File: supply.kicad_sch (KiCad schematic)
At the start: 0 parts

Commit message: added hierachical sheets
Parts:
- added C1, C2, C5, C6, C7, C8: C_Small, symbol Device:C_Small
- added IC3: BQ25622ERYKR, ARMband:BQ25620RYKR, symbol ARMband:BQ25622ERYKR
- added IC4: BQ27427YZFR, ARMband:BGA9C50P3X3_158X162X62, symbol ARMband:BQ27427YZFR
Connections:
- new net +1V8: C7.1, C8.1
- new net +3V3: C5.1, C6.1
- new net +5V: C1.1, C2.1
- new net CHRG_CE: IC3.14 (~{CE})
- new net CHRG_INT: IC3.11 (~{INT})
- new net CHRG_PG: IC3.3 (~{PG})
- new net CHRG_STAT: IC3.10 (STAT)
- new net GASG_BIN: IC4.B1 (BIN)
- new net GASG_GPOUT: IC4.A1 (GPOUT)
- new net GND: C1.2, C2.2, C5.2, C6.2, C7.2, C8.2, IC3.15 (GND), IC4.B2 (VSS_1), IC4.C1 (VSS_2)
- new net I2C_SCL: IC3.13 (SCL), IC4.A3 (SCL)
- new net I2C_SDA: IC3.12 (SDA), IC4.A2 (SDA)

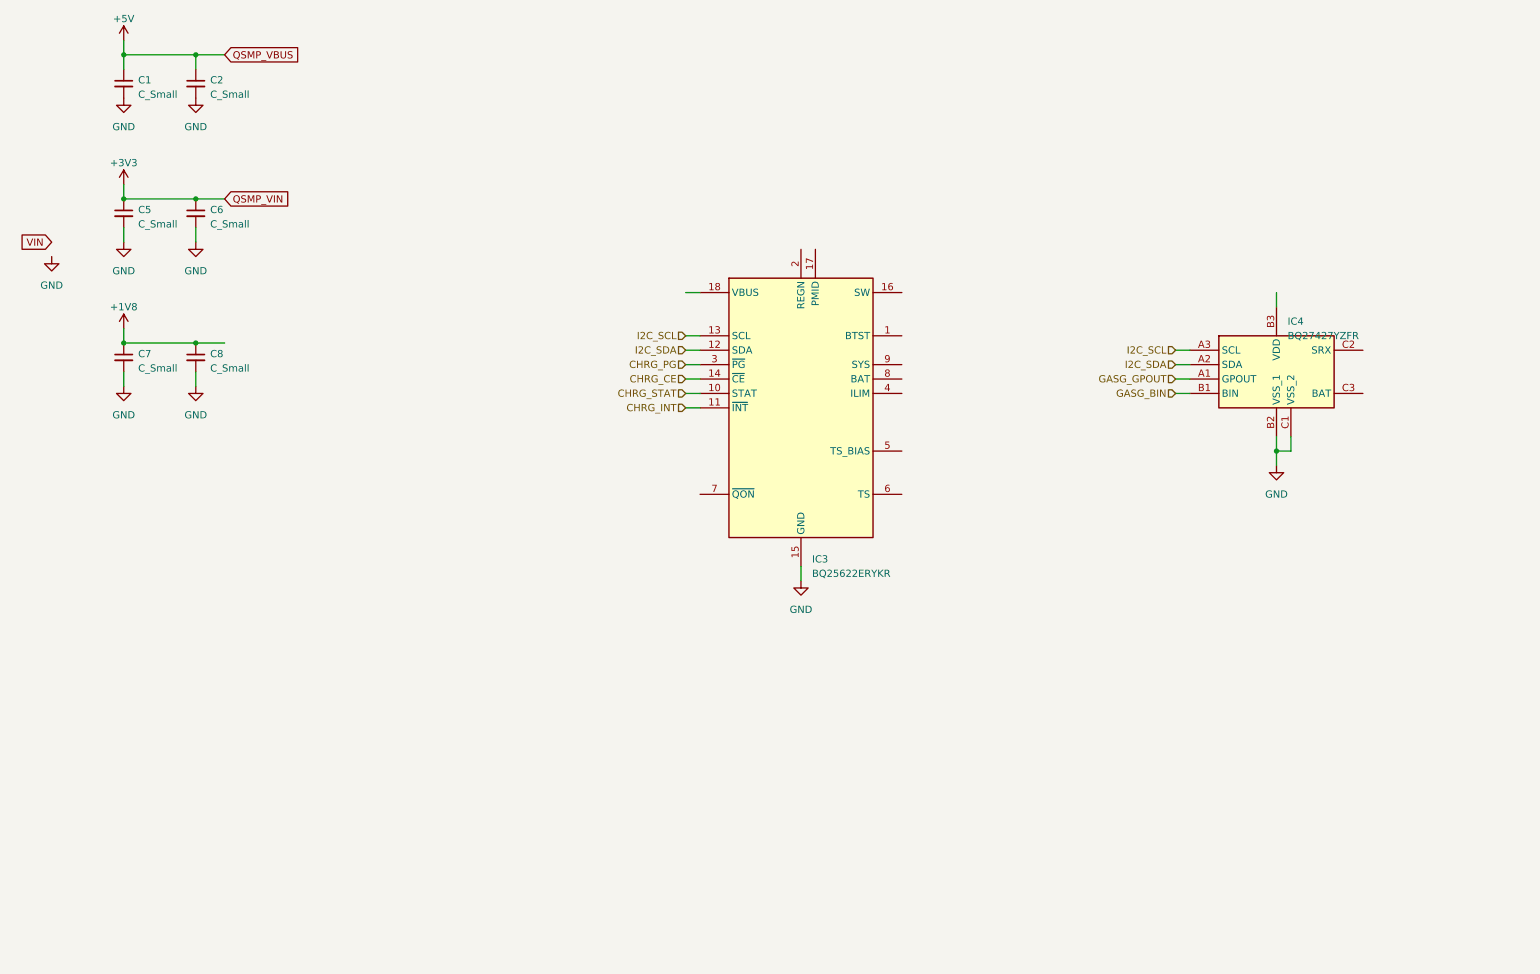
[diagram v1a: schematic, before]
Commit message: progressed charging and gas gauge schematic
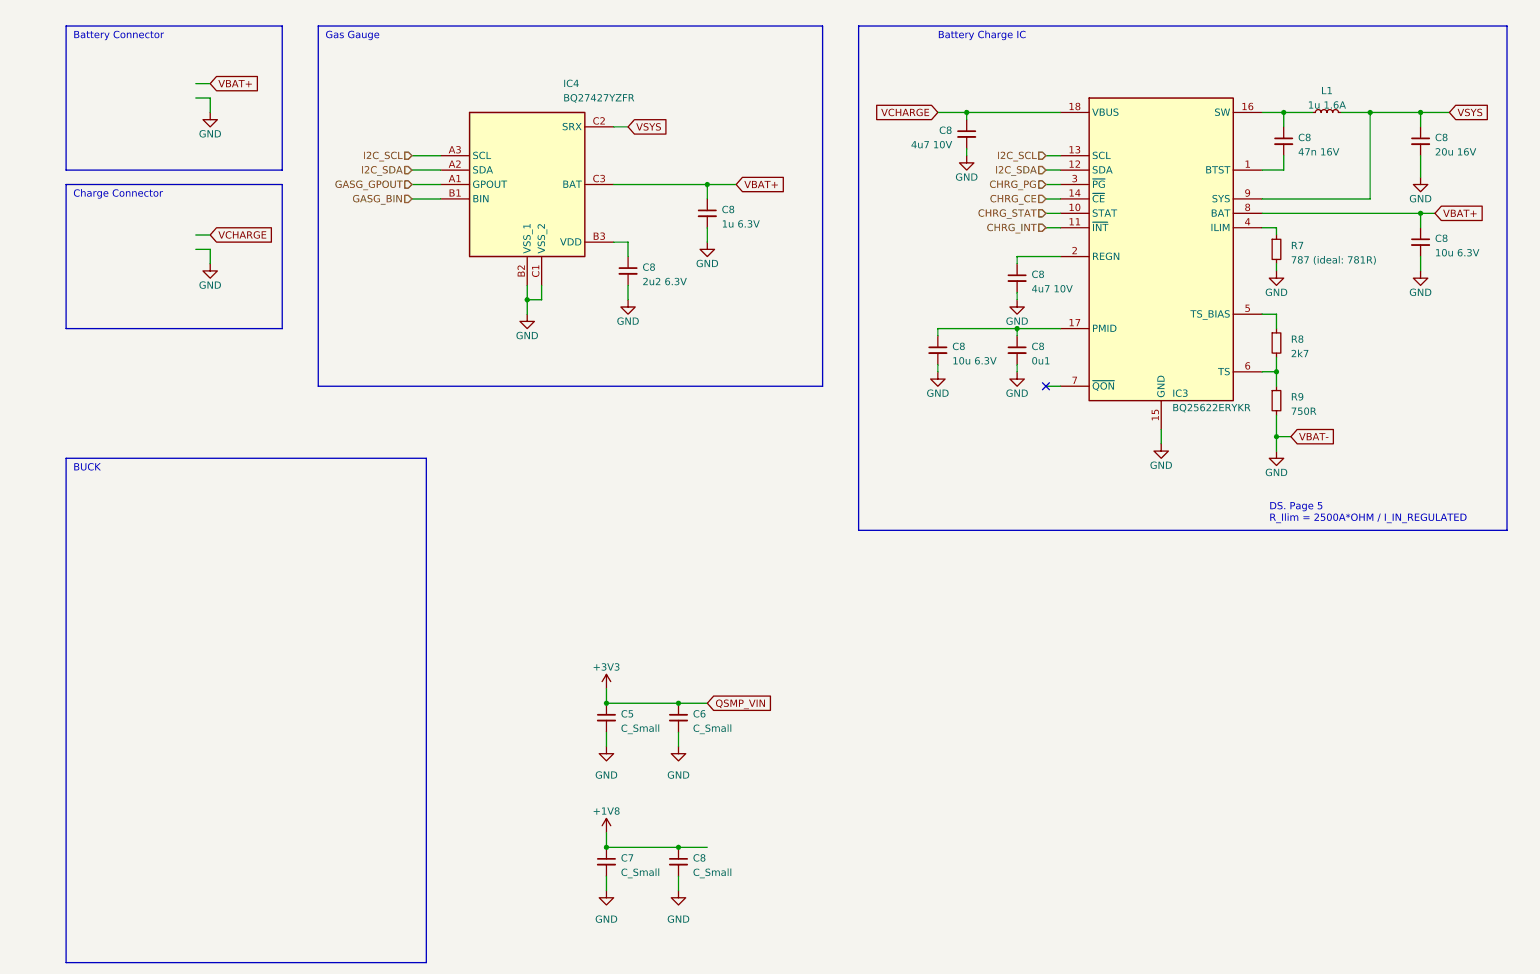
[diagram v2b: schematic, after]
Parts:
- removed C1, C2: C_Small, symbol Device:C_Small
- added C8: 20u 16V, ARMband:C_0704, symbol Device:C_Small
- added C8: 0u1, symbol Device:C_Small
- added C8: 47n 16V, Capacitor_SMD:C_0201_0603Metric, symbol Device:C_Small
- added C8 (x2): 4u7 10V, Capacitor_SMD:C_0402_1005Metric, symbol Device:C_Small
- added C8: 2u2 6.3V, Capacitor_SMD:C_0201_0603Metric, symbol Device:C_Small
- added C8 (x2): 10u 6.3V, Capacitor_SMD:C_0402_1005Metric, symbol Device:C_Small
- added C8: 1u 6.3V, Capacitor_SMD:C_0201_0603Metric, symbol Device:C_Small
- added L1: 1u 1.6A, Inductor_SMD:L_0603_1608Metric, symbol Device:L_Small
- added R7: 787 (ideal: 781R), Resistor_SMD:R_0201_0603Metric, symbol Device:R_Small
- added R8: 2k7, symbol Device:R_Small
- added R9: 750R, symbol Device:R_Small
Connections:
- net GND: now also C8.2, C8.2, C8.2, C8.2, C8.2, C8.2, C8.2, C8.2, R7.2, R9.2
- net at IC4.B3 (VDD): now also C8.1
- net VSYS: now reaches IC4.C2 (SRX)
- net VSYS: now also IC3.9 (SYS), C8.1, L1.2
- net VBAT+: now reaches IC4.C3 (BAT)
- net VBAT+: now also IC3.8 (BAT), C8.1, C8.1
- net at IC3.1 (BTST): now also C8.2
- net at IC3.16 (SW): now also C8.1, L1.1
- net at IC3.17 (PMID): now also C8.1, C8.1
- net VCHARGE: now reaches IC3.18 (VBUS)
- net VCHARGE: now also C8.1
- net at IC3.2 (REGN): now also C8.1
- net at IC3.4 (ILIM): now also R7.1
- net at IC3.5 (TS_BIAS): now also R8.1
- net at IC3.6 (TS): now also R8.2, R9.1
- no-connect marks 0 -> 1
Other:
- note added: "BUCK"
- note added: "Battery Charge IC"
- note added: "Battery Connector"
- note added: "Charge Connector"
- note added: "DS. Page 5 R_Ilim = 2500A*OHM / I_IN_REGULATED"
- note added: "Gas Gauge"
- moved on the sheet: C5, C6, C7, C8, IC3, IC4

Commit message: added buck
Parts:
- removed C5, C6, C7, C8: C_Small, symbol Device:C_Small
- added C7 (x2): 22u, symbol Device:C_Small
- added C7: 22u, Capacitor_SMD:C_0402_1005Metric, symbol Device:C_Small
- added IC3: TPS62410DRCR, ARMband:LM5165XQDRCRQ1, symbol ARMband:TPS62410DRCR
- added L1, L2: 4u7, Inductor_SMD:L_Bourns-SRN4018, symbol Device:L_Small
- added R10: 180k, Resistor_SMD:R_0201_0603Metric, symbol Device:R_Small
- added R14: 0R, Resistor_SMD:R_0201_0603Metric, symbol Device:R_Small
- added R2 (x2): 10k, Resistor_SMD:R_0201_0603Metric_Pad0.64x0.40mm_HandSolder, symbol Device:R_Small
- added R7: 680k, Resistor_SMD:R_0201_0603Metric, symbol Device:R_Small
- added R8: 150k, Resistor_SMD:R_0201_0603Metric, symbol Device:R_Small
- added R9: 360k, Resistor_SMD:R_0201_0603Metric, symbol Device:R_Small
- renumbered L1 to L3, R7 to R11, R8 to R12, R9 to R13
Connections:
- net +1V8: now also C7.1, C7.1, L2.1, R9.1
- net +3V3: now also C7.1, IC3.4 (FB1), L1.1, R7.1
- net GND: now also C7.2, C7.2, IC3.11 (EP_1), IC3.12 (EP_2), IC3.13 (EP_3), IC3.14 (EP_4), IC3.15 (EP_5), IC3.8 (GND), R10.2, R14.2, R8.2
- net VSYS: now also IC3.3 (VIN), R2.1, R2.1
- new net: IC3.7 (EN1), R2.2
- new net: C7.2, IC3.1 (ADJ2), R10.1, R9.2
- new net: IC3.2 (MODE/DATA), R14.1
- new net: IC3.10 (SW2), L2.2
- new net: IC3.5 (DEF_1), R7.2, R8.1
- new net: IC3.6 (SW1), L1.2
- new net: IC3.9 (EN2), R2.2
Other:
- note added: "Vref = 0.6V 1.8V Rail probably heavy ripple current due to low load"

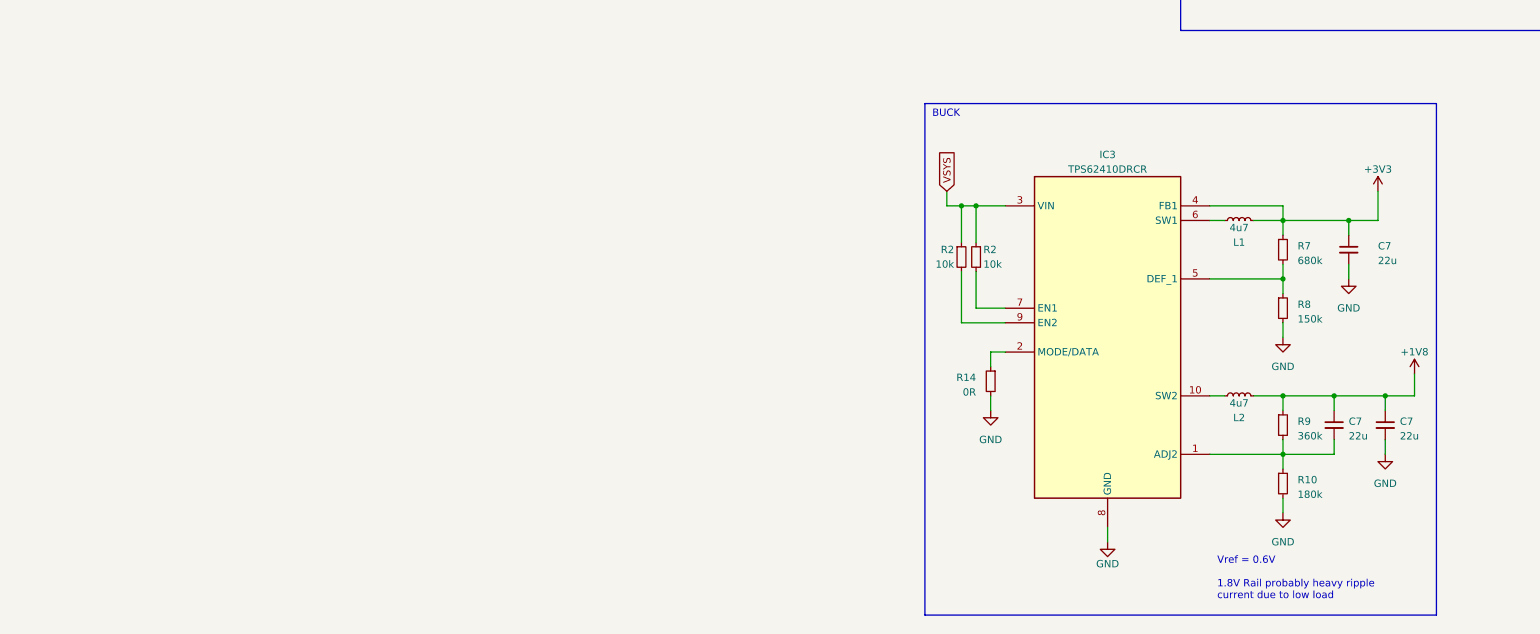
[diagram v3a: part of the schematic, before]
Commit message: added new bucks
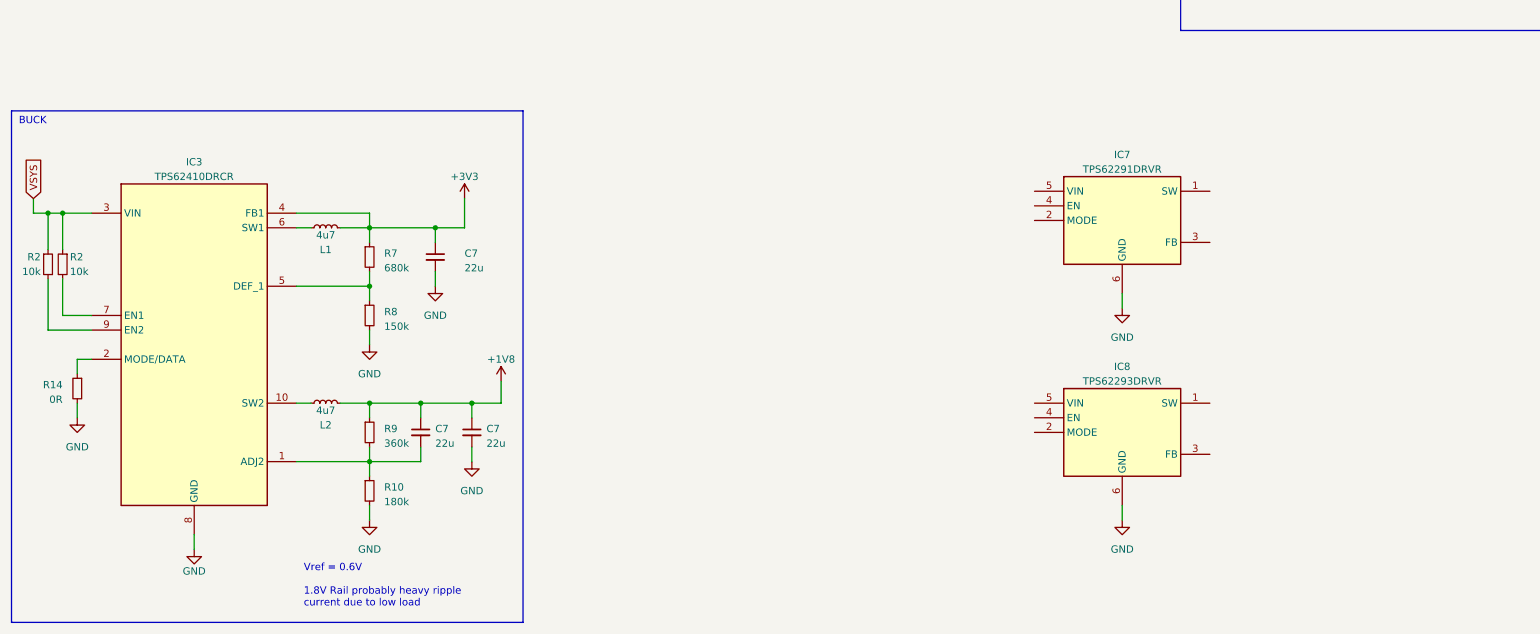
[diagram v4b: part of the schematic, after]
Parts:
- added IC7: TPS62291DRVR, ARMband:SON65P200X200X80-7N, symbol ARMband:TPS62291DRVR
- added IC8: TPS62293DRVR, ARMband:SON65P200X200X80-7N, symbol ARMband:TPS62293DRVR
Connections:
- net GND renamed EP
- net EP: now also IC7.6 (GND), IC7.7 (EP), IC8.6 (GND), IC8.7 (EP)
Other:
- moved on the sheet: C7, IC3, L1, L2, R10, R14, R2, R7, R8, R9

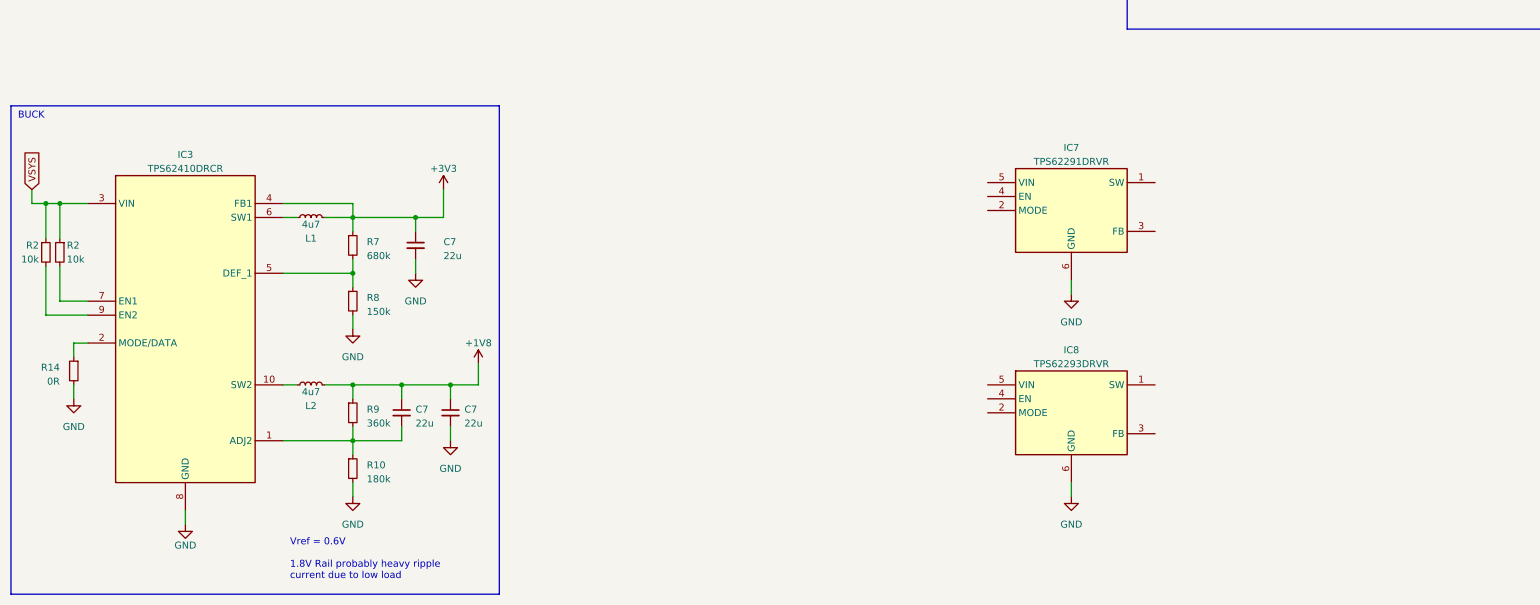
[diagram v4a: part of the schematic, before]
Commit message: buck circuits
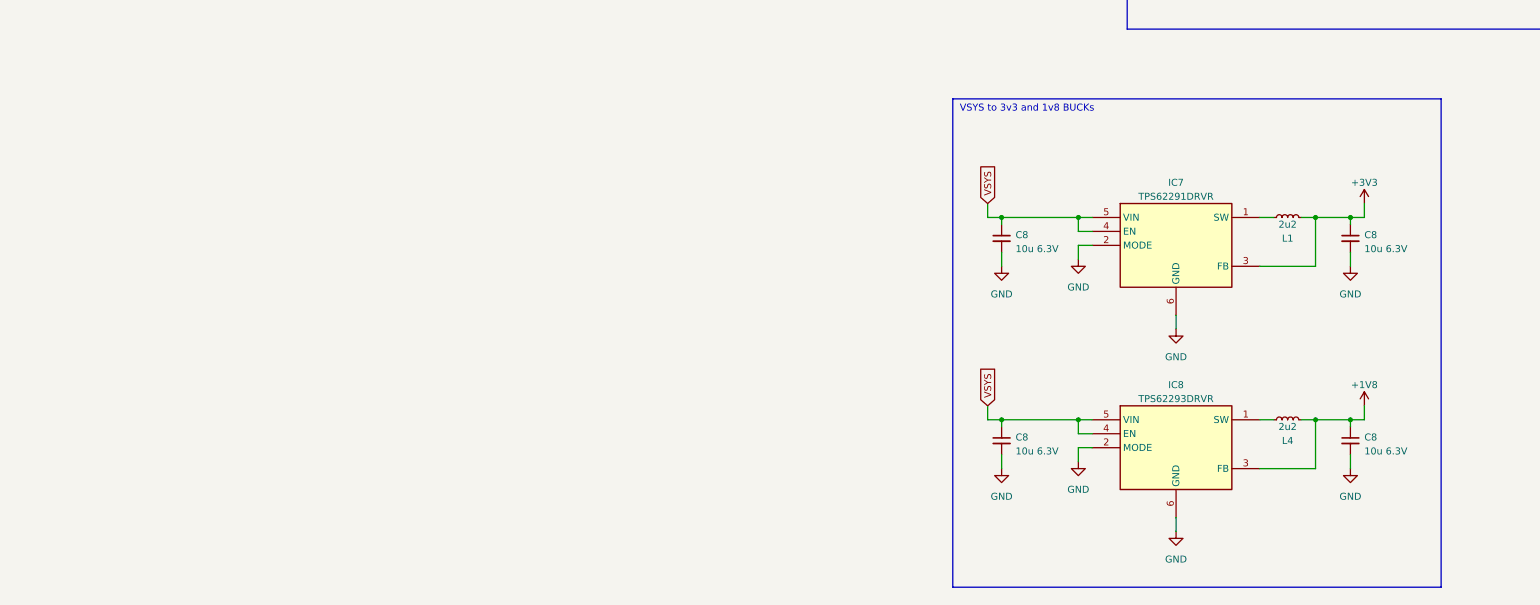
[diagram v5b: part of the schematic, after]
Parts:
- removed C7 (x2): 22u, symbol Device:C_Small
- removed C7: 22u, Capacitor_SMD:C_0402_1005Metric, symbol Device:C_Small
- removed IC3: TPS62410DRCR, ARMband:LM5165XQDRCRQ1, symbol ARMband:TPS62410DRCR
- removed L2: 4u7, Inductor_SMD:L_Bourns-SRN4018, symbol Device:L_Small
- removed R10: 180k, Resistor_SMD:R_0201_0603Metric, symbol Device:R_Small
- removed R14: 0R, Resistor_SMD:R_0201_0603Metric, symbol Device:R_Small
- removed R2 (x2): 10k, Resistor_SMD:R_0201_0603Metric_Pad0.64x0.40mm_HandSolder, symbol Device:R_Small
- removed R7: 680k, Resistor_SMD:R_0201_0603Metric, symbol Device:R_Small
- removed R8: 150k, Resistor_SMD:R_0201_0603Metric, symbol Device:R_Small
- removed R9: 360k, Resistor_SMD:R_0201_0603Metric, symbol Device:R_Small
- added C8 (x4): 10u 6.3V, Capacitor_SMD:C_0402_1005Metric, symbol Device:C_Small
- added L4: 2u2, symbol Device:L_Small
- L1: value 4u7 -> 2u2; footprint Inductor_SMD:L_Bourns-SRN4018 -> (none); MFN 652-SRN4026-4R7M -> 81-LQM2MPN2R2MG0L
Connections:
- net +1V8: now also IC8.3 (FB), C8.1, L4.1
- net +3V3: now also IC7.3 (FB), C8.1
- net EP: now also IC7.2 (MODE), IC8.2 (MODE), C8.2, C8.2, C8.2, C8.2
- net VSYS: now also IC7.4 (EN), IC7.5 (VIN), IC8.4 (EN), IC8.5 (VIN), C8.1, C8.1
- net at IC8.1 (SW): now also L4.2
- net at IC7.1 (SW): now also L1.2
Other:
- note added: "VSYS to 3v3 and 1v8 BUCKs"
- note removed: "BUCK"
- note removed: "Vref = 0.6V 1.8V Rail probably heavy ripple current due to low load"
- moved on the sheet: IC7, IC8, L1

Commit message: Add Inductor LQM2MPN2R2MG0L
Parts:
- L1, L4: footprint (none) -> ARMband:LQM2MPN1R0NG0L
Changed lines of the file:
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@@
       (effects (font (size 1.27 1.27)))
     )
-    (property "Footprint" "" (at 99.06 123.19 0)
+    (property "Footprint" "ARMband:LQM2MPN1R0NG0L" (at 99.06 123.19 0)
       (effects (font (size 1.27 1.27)) hide)
     )
@@
       (effects (font (size 1.27 1.27)))
     )
-    (property "Footprint" "" (at 99.06 160.02 0)
-      (effects (font (size 1.27 1.27)) hide)
-    )
+    (property "Footprint" "ARMband:LQM2MPN1R0NG0L" (at 99.06 160.02 0)
+      (effects (font (size 1.27 1.27)) hide)
+    )
